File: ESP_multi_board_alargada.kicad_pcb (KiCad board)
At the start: 2 copper layers, 24 parts, among them P101 CONN_01X02, P102 CONN_01X06, P103 CONN_01X02, P104 CONN_01X06, P105 CONN_01X12, P106 CONN_01X03, P107 CONN_I2C_MPU6050, P108 CONN_PINES_DIG, SW101 SW_PUSH_SMALL, SW102 SWITCH_INV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

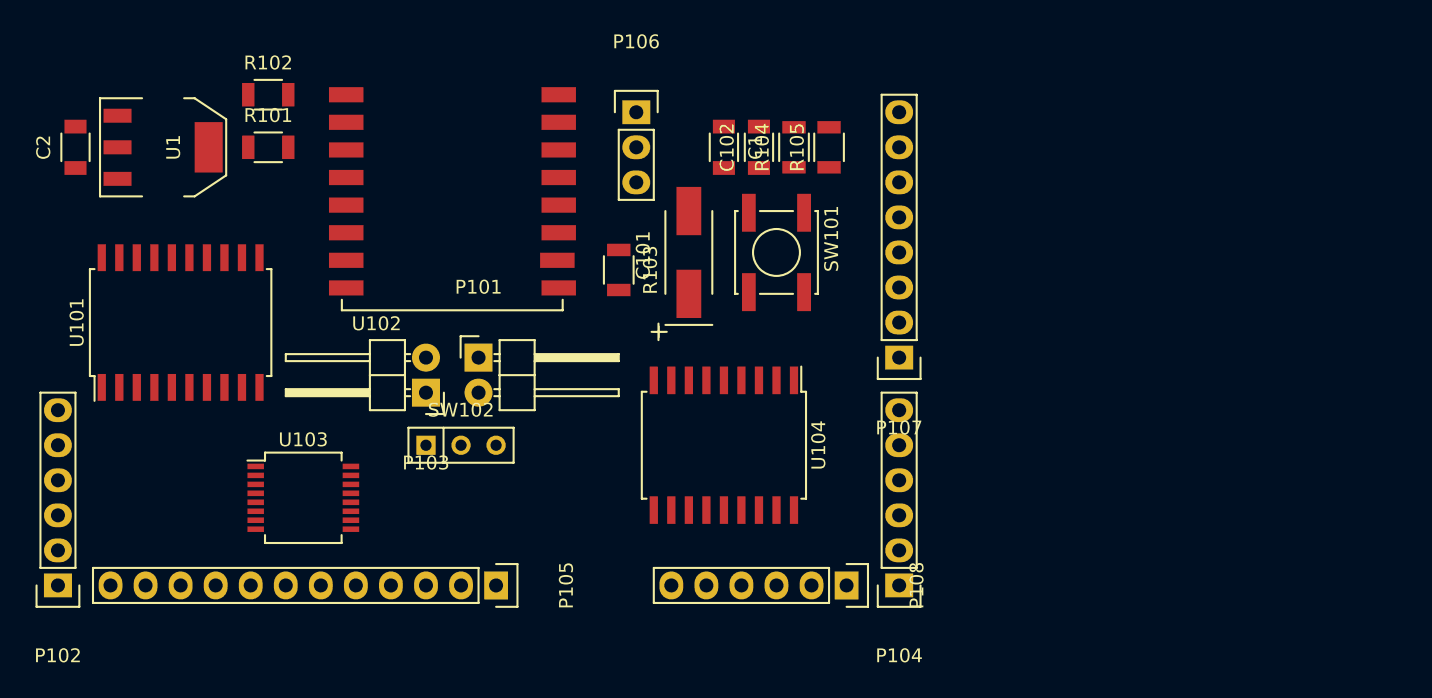
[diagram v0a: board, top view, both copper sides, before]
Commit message: incluida version de la placa alargada 10x2.5 cm
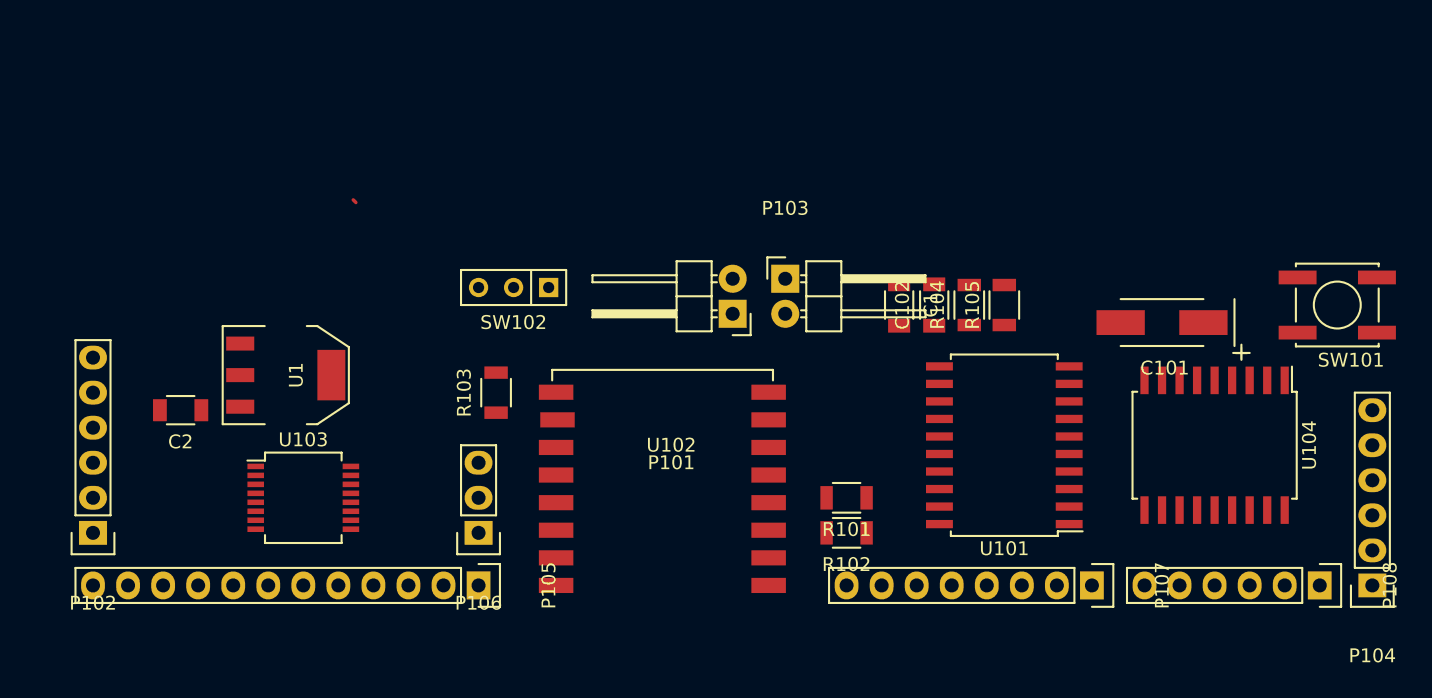
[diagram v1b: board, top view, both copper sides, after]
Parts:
- moved U101 60.3 mm to (191.8, 83.8), turned to 180 degrees
- moved R102 52.6 mm to (180.3, 90.2), turned to 180 degrees
- moved R101 49.0 mm to (180.3, 87.6), turned to 180 degrees
- moved U102 46.0 mm to (174.0, 94.0), turned to 180 degrees
- moved SW101 40.8 mm to (215.9, 73.7), turned to 180 degrees
- moved U104 35.6 mm to (207.0, 83.8)
- moved C101 34.7 mm to (203.2, 74.9), turned to 180 degrees
- moved P104 34.3 mm to (218.4, 94.0)
- moved P108 34.3 mm to (214.6, 94.0)
- moved P106 32.6 mm to (153.7, 90.2), turned to 180 degrees
- moved P103 27.3 mm to (175.9, 71.8), turned to 0 degrees
- moved P107 21.6 mm to (198.1, 94.0), turned to 270 degrees
- moved C2 20.5 mm to (132.1, 81.3), turned to 180 degrees
- moved U1 18.8 mm to (139.7, 78.7)
- moved P101 18.7 mm to (172.1, 74.3), turned to 180 degrees
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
